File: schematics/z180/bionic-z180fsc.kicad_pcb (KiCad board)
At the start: 2 copper layers, 25.4 x 68.6 mm, 11 parts, among them J1 Bionic-P135, J2 Bionic-P245, U1 Z80180FSC, U2 11AA010-I/TT, U3 74AHCT157

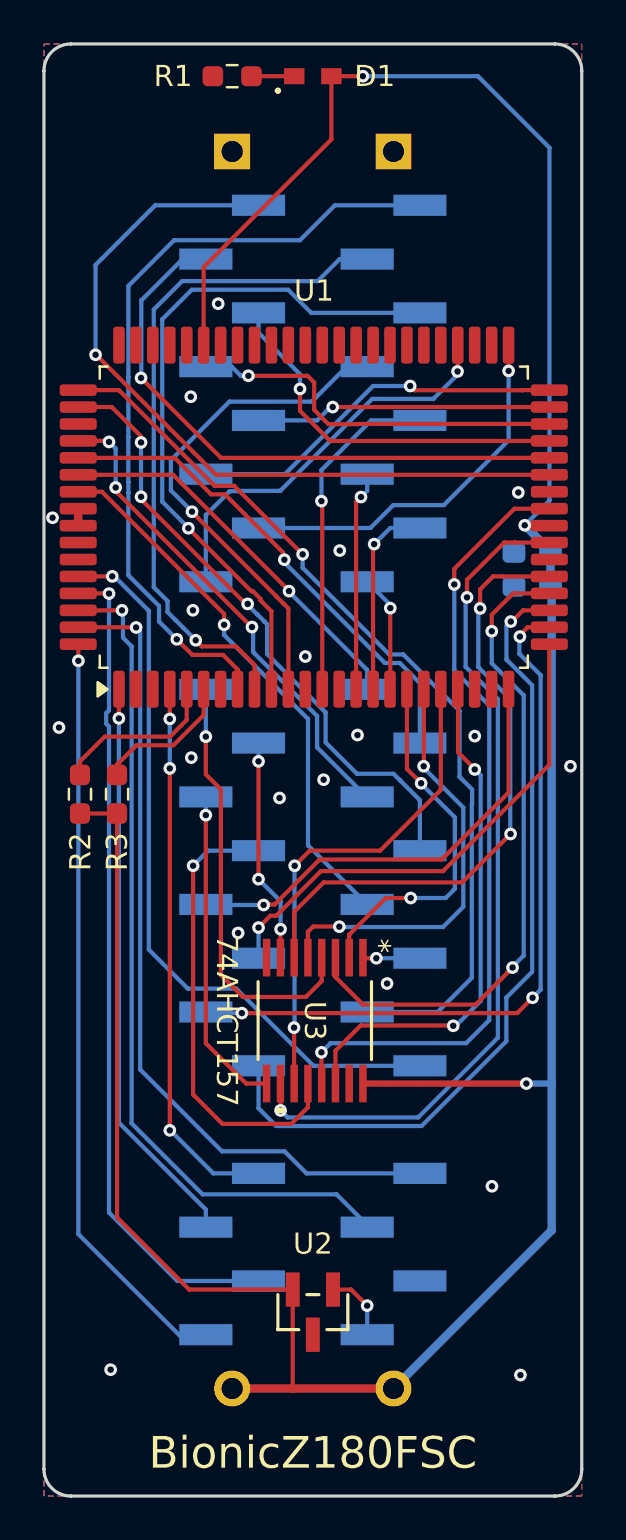
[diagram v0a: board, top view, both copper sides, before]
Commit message: [Z180] Optimze QFP board layout
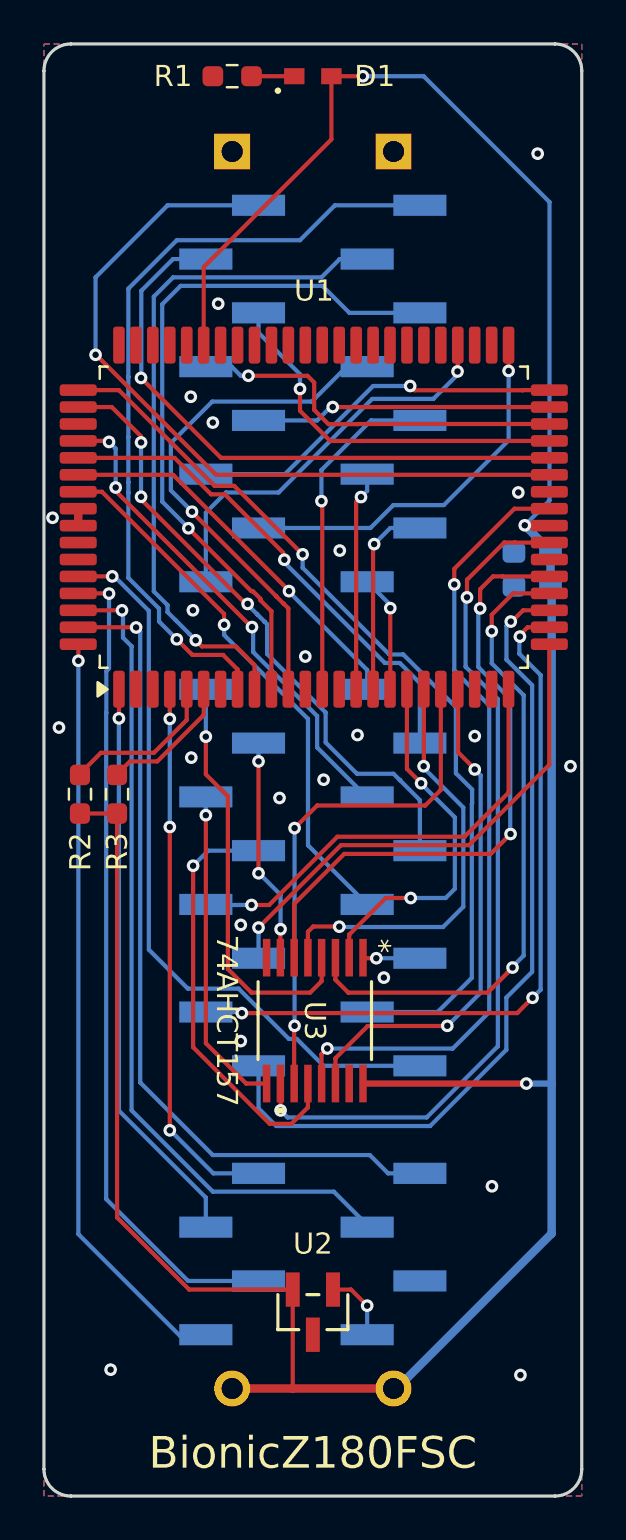
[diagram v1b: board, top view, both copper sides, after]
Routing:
- net VCC: track 142.5 -> 141.1 mm
- net P33: track 21.6 -> 20.3 mm
- net A10: track 23.4 -> 24.5 mm
- net A2: track 32.8 -> 33.4 mm
- net P30: track 20.4 -> 19.9 mm
- net GND: vias 19 -> 22
